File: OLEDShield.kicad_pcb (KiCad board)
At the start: 2 copper layers, 68.6 x 53.3 mm, 252 parts, among them P1 CONN_5X2, P2 CONN_5X2, P3 CONN_1, P4 CONN_1, P5 CONN_1, SW1 SW_PUSHBUTTON

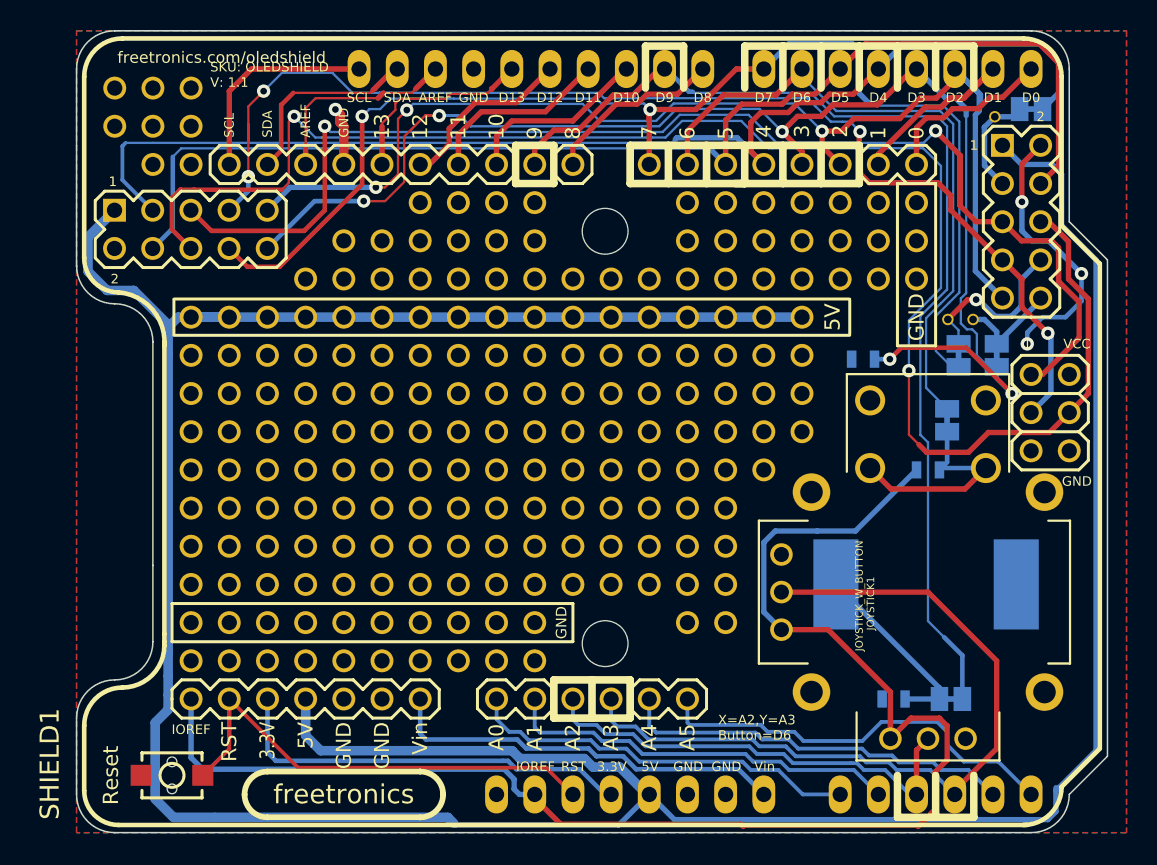
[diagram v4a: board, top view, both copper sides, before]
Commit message: Mild cleanup for 1.2 - deepen cutout for Ethernet models, add NC breakout hole, tidy up, swap X axis polarity
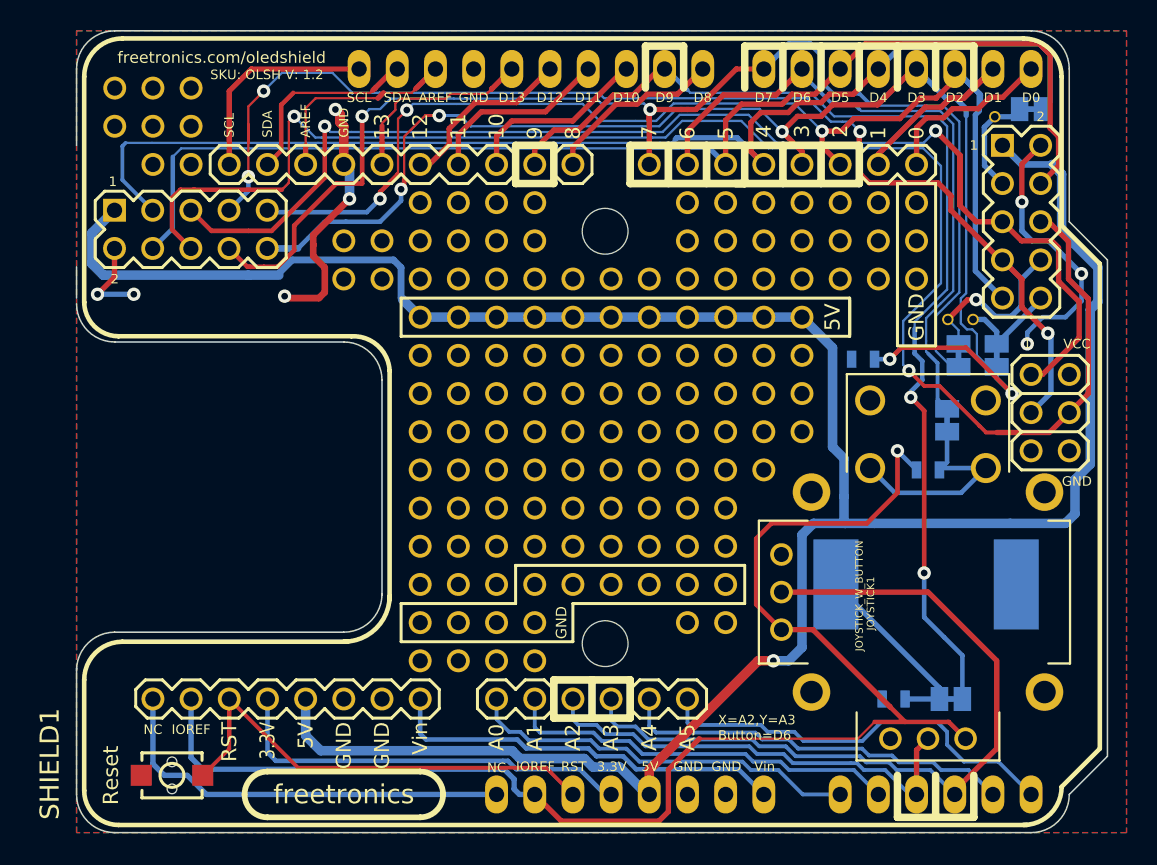
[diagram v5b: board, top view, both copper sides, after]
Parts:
- removed the 1PIN at (205.7, 129.5)
- removed the 1PIN at (218.4, 142.2)
- removed the 1PIN at (218.4, 134.6)
- removed the 1PIN at (218.4, 137.2)
- removed the 1PIN at (218.4, 139.7)
- removed the 1PIN at (215.9, 134.6)
- removed the 1PIN at (213.4, 134.6)
- removed the 1PIN at (213.4, 127.0)
- removed the 1PIN at (210.8, 134.6)
- removed the 1PIN at (208.3, 134.6)
- removed the 1PIN at (205.7, 134.6)
- removed the 1PIN at (205.7, 132.1)
- removed the 1PIN at (208.3, 132.1)
- removed the 1PIN at (210.8, 132.1)
- removed the 1PIN at (213.4, 132.1)
- removed the 1PIN at (215.9, 132.1)
- removed the 1PIN at (210.8, 129.5)
- removed the 1PIN at (205.7, 149.9)
- removed the 1PIN at (205.7, 137.2)
- removed the 1PIN at (208.3, 137.2)
- removed the 1PIN at (210.8, 137.2)
- removed the 1PIN at (213.4, 137.2)
- removed the 1PIN at (215.9, 137.2)
- removed the 1PIN at (208.3, 129.5)
- removed the 1PIN at (218.4, 132.1)
- removed the 1PIN at (215.9, 139.7)
- removed the 1PIN at (213.4, 139.7)
- removed the 1PIN at (210.8, 139.7)
- removed the 1PIN at (208.3, 139.7)
- removed the 1PIN at (205.7, 139.7)
- removed the 1PIN at (205.7, 142.2)
- removed the 1PIN at (208.3, 142.2)
- removed the 1PIN at (210.8, 142.2)
- removed the 1PIN at (213.4, 142.2)
- removed the 1PIN at (215.9, 142.2)
- removed the 1PIN at (215.9, 129.5)
- removed the 1PIN at (213.4, 129.5)
- removed the 1PIN at (218.4, 129.5)
- removed the 1PIN at (238.8, 147.3)
- removed the 1PIN at (241.3, 147.3)
- removed the 1PIN at (236.2, 147.3)
- removed the 1PIN at (218.4, 152.4)
- removed the 1PIN at (215.9, 152.4)
- removed the 1PIN at (213.4, 152.4)
- removed the 1PIN at (210.8, 152.4)
- removed the 1PIN at (208.3, 152.4)
- removed the 1PIN at (205.7, 152.4)
- removed the 1PIN at (215.9, 147.3)
- removed the 1PIN at (213.4, 147.3)
- removed the 1PIN at (210.8, 147.3)
- removed the 1PIN at (208.3, 147.3)
- removed the 1PIN at (205.7, 147.3)
- removed the 1PIN at (205.7, 144.8)
- removed the 1PIN at (208.3, 144.8)
- removed the 1PIN at (210.8, 144.8)
- removed the 1PIN at (213.4, 144.8)
- removed the 1PIN at (215.9, 144.8)
- removed the 1PIN at (233.7, 147.3)
- removed the 1PIN at (231.1, 147.3)
- removed the 1PIN at (228.6, 147.3)
- removed the 1PIN at (218.4, 147.3)
- removed the 1PIN at (218.4, 144.8)
- added 1PIN: P***, 1pin_prototyping, F.Cu at (203.2, 154.9)
- added 1PIN: P***, 1pin_prototyping, F.Cu at (221.0, 149.9)
- moved 1PIN 33.1 mm to (241.3, 147.3)
- moved 1PIN 28.1 mm to (238.8, 147.3)
- moved 1PIN 23.0 mm to (236.2, 147.3)
- moved 1PIN 18.0 mm to (233.7, 147.3)
- moved 1PIN 13.0 mm to (231.1, 147.3)
- moved 1PIN 8.03 mm to (228.6, 147.3)
- moved Ref** 1.88 mm to (200.7, 157.1)
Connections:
- JOYSTICK1 pad Y1: VCC -> GND
- JOYSTICK1 pad Y3: GND -> VCC
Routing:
- net +5V: track 232.8 -> 174.0 mm, vias 0 -> 1
- net N-0000038: track 0.00 -> 28.0 mm
- net GND: track 27.9 -> 46.7 mm, vias 4 -> 8
- net VCC: track 99.0 -> 95.2 mm, vias 0 -> 1
- net /OLED_nCS: track 88.1 -> 84.7 mm
- net /MOSI: track 107.8 -> 104.5 mm
- net /OLED_nRST: track 92.9 -> 95.6 mm
- net /MISO: track 86.4 -> 85.1 mm
- net /D9: track 72.2 -> 73.2 mm, vias 0 -> 2
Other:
- outline, holes or cut-outs redrawn
- board text added: "NC"
- board text added: "SKU: OLSH V: 1.2"
- board text removed: "SKU: OLEDSHIELD V: 1.1"
